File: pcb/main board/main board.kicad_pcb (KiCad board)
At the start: 2 copper layers, 110 x 155 mm, 71 parts, among them J1 Motor 0 Conn, J10 12V Battery, J11 BAU, J12 Servo 4 Conn, J13 Servo 1 Conn, J14 Servo 2 Conn, J15 Servo 3 Conn, J16 Servo 5 Conn, J17 Servo 6 Conn, J18 Servo 7 Conn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

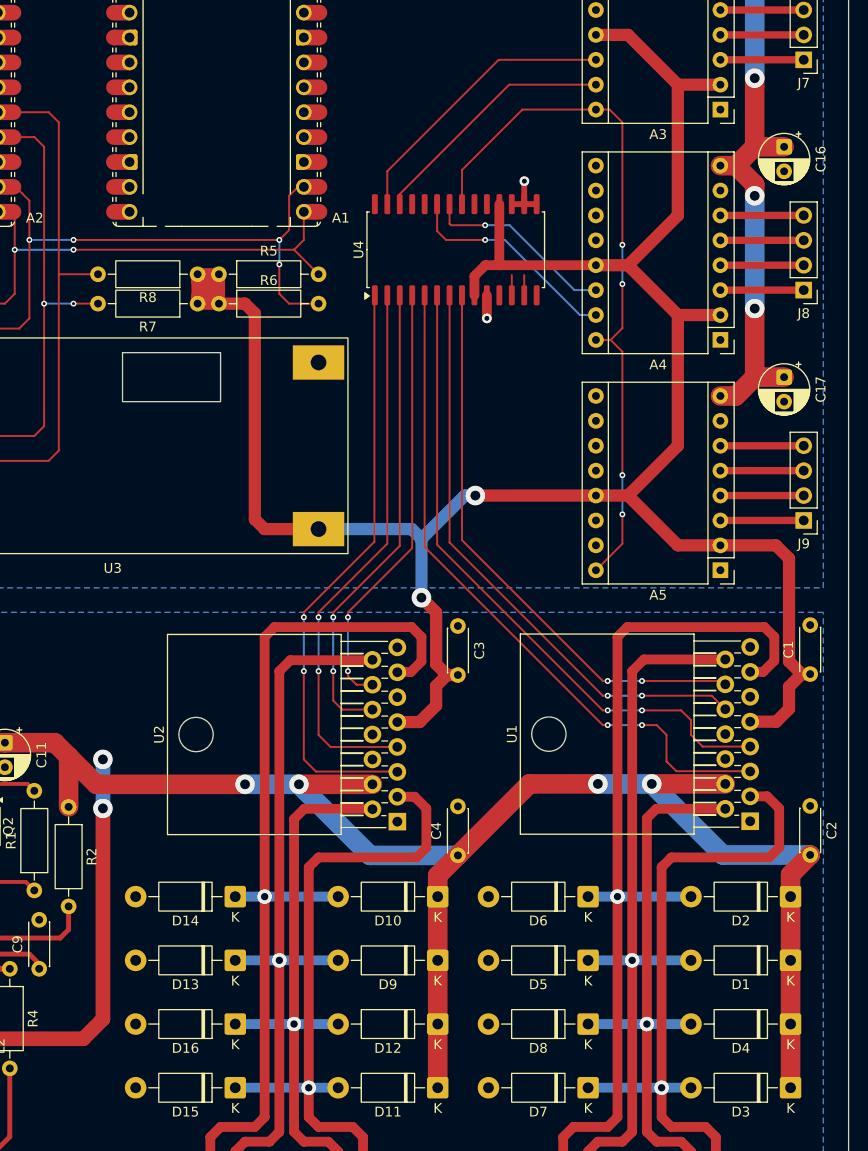
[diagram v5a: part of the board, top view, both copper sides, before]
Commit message: Replaced L298Ns footprints to a vertical version and almost finished rewiring them...
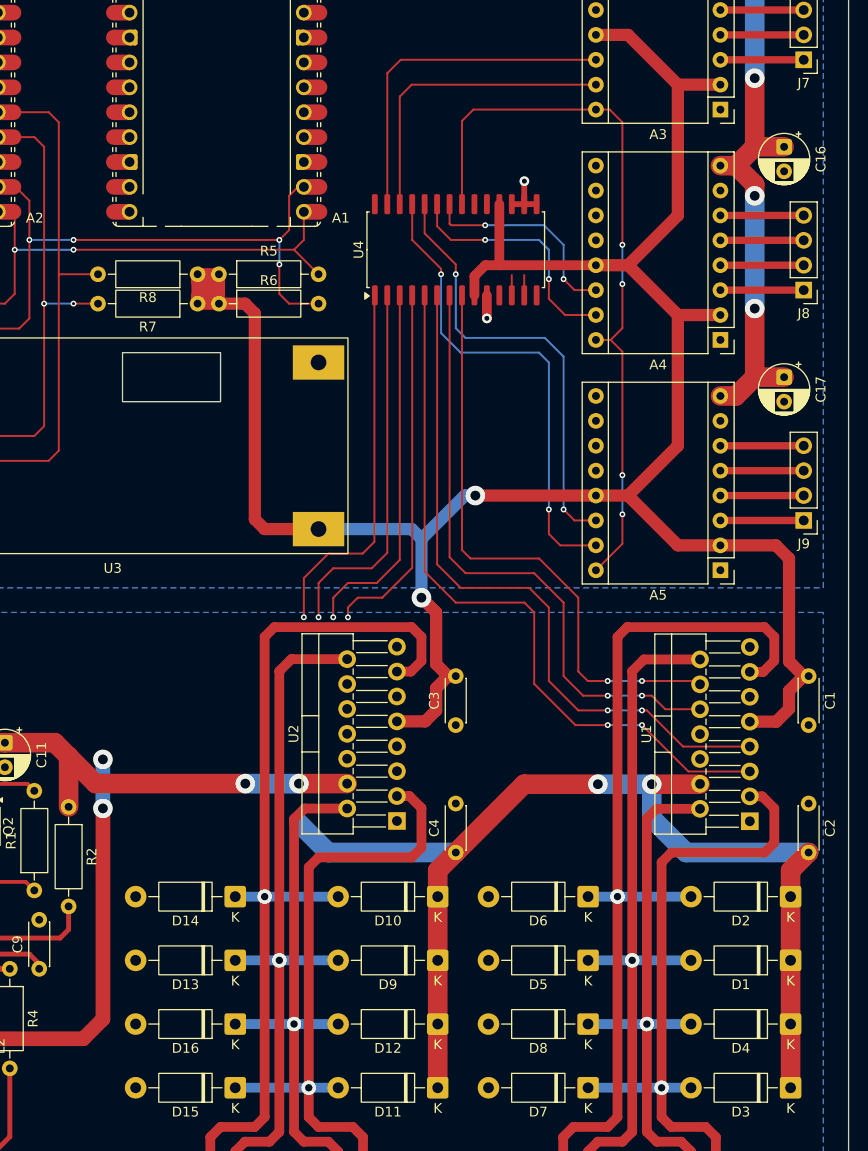
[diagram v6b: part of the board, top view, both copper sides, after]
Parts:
- U1, U2: footprint Package_TO_SOT_THT:TO-220-15_P2.54x2.54mm_StaggerOdd_Lead5.84mm_TabDown -> Package_TO_SOT_THT:TO-220-15_P2.54x5.08mm_StaggerOdd_Lead4.58mm_Vertical
- moved C3 10.1 mm to (247.5, 172.5), turned to 90 degrees
- moved C4 0.37 mm to (247.5, 185.5)
- moved C2 0.30 mm to (283.5, 180.5)
- moved C1 0.26 mm to (283.5, 167.5), turned to -90 degrees
- moved U2 0.08 mm to (241.5, 182.3)
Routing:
- net Stepper 3 Step: track 0.00 -> 49.4 mm, vias 0 -> 2
- net Stepper 3 Sleep: track 0.00 -> 45.5 mm, vias 0 -> 2
- net Motor 3 Direction Pin 1: track 60.4 -> 37.9 mm, vias 2 -> 1
- net Motor 3 Direction Pin 2: track 56.3 -> 38.1 mm, vias 2 -> 1
- net Motor 4 Direction Pin 1: track 48.5 -> 37.4 mm, vias 2 -> 1
- net Motor 4 Direction Pin 2: track 44.4 -> 37.0 mm, vias 2 -> 1
- net Stepper 1 Sleep: track 29.4 -> 35.2 mm
- net Stepper 1 Step: track 25.7 -> 31.5 mm
- net +12V: track 311.4 -> 306.4 mm
- net Motor 1 Direction Pin 2: track 66.8 -> 71.3 mm
- net Motor 1 Direction Pin 1: track 70.0 -> 73.9 mm
- net Steppers Dir: track 72.3 -> 75.2 mm
- net Net-(D1-A): track 74.8 -> 72.1 mm
- net Stepper 2 Step: track 22.5 -> 25.1 mm, vias 1 -> 2
- net Net-(D4-A): track 58.2 -> 55.6 mm
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
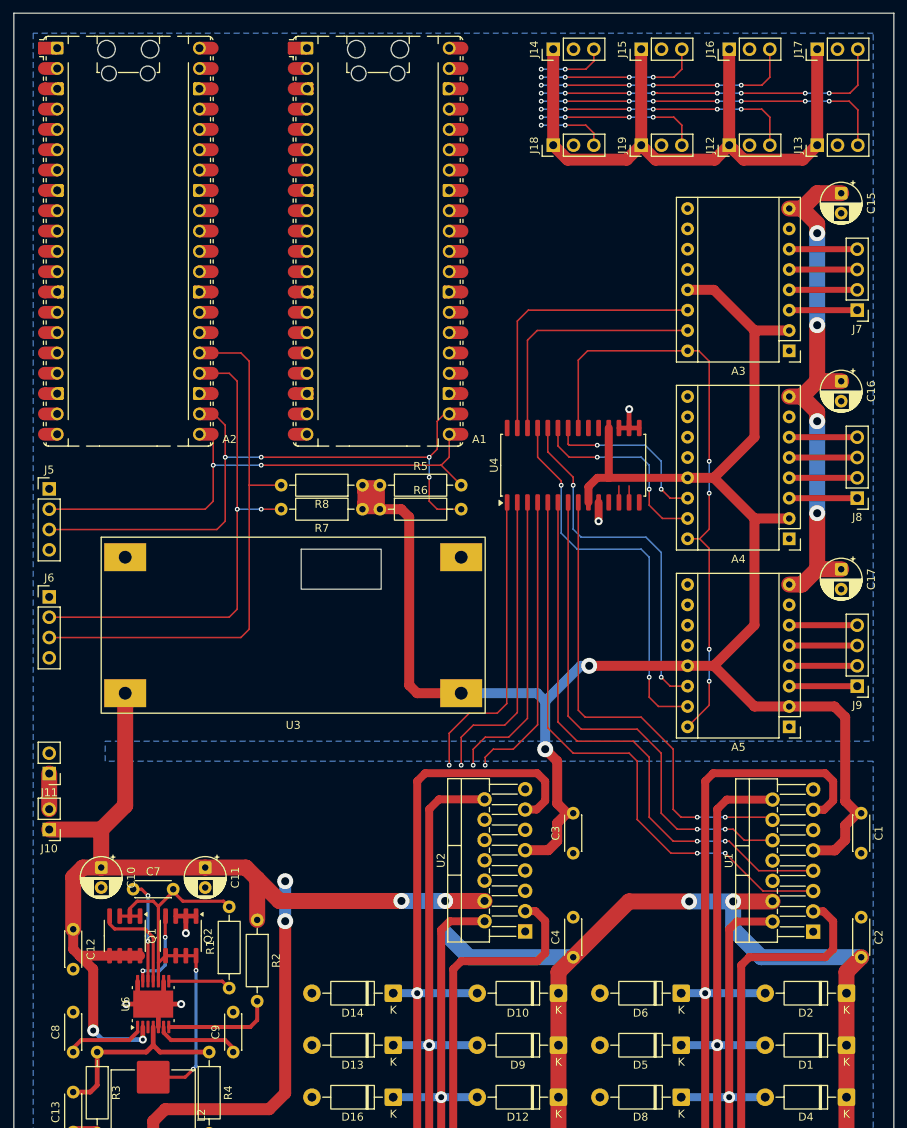
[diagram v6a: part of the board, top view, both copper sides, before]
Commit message: Changed largeur of pistes and finished rewiring DC motors drivers
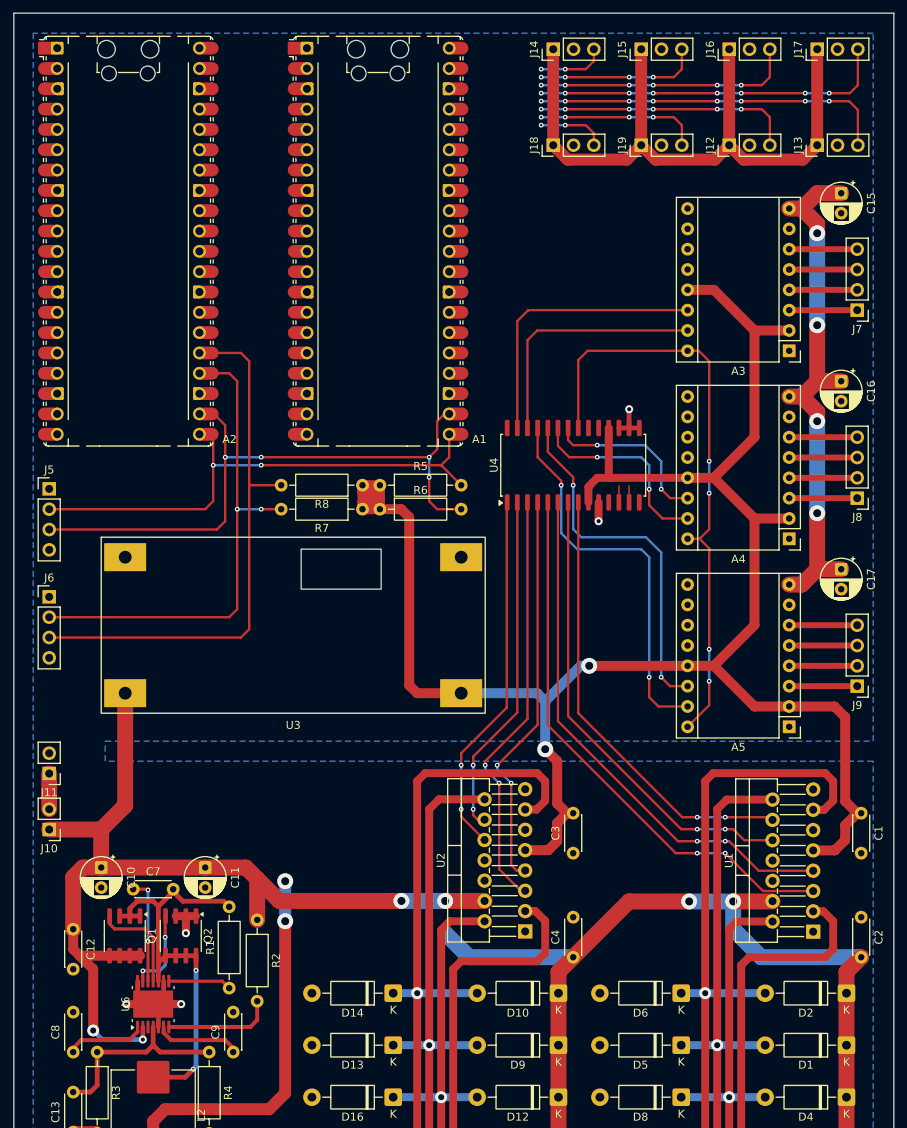
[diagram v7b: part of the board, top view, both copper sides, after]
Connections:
- U4 pad 1: Motor 3 Direction Pin 1 -> Motor 4 Direction Pin 1
- U4 pad 2: Motor 3 Direction Pin 2 -> Motor 4 Direction Pin 2
- U4 pad 3: Motor 4 Direction Pin 1 -> Motor 3 Direction Pin 1
- U4 pad 4: Motor 4 Direction Pin 2 -> Motor 3 Direction Pin 2
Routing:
- net Motor 3 Direction Pin 1: track 37.9 -> 53.1 mm, vias 1 -> 2
- net Motor 3 Direction Pin 2: track 38.1 -> 50.2 mm, vias 1 -> 2
- net Motor 4 Direction Pin 1: track 37.4 -> 45.8 mm, vias 1 -> 2
- net Motor 4 Direction Pin 2: track 37.0 -> 43.0 mm, vias 1 -> 2
- net Motor 1 Direction Pin 1: track 73.9 -> 69.5 mm
- net Motor 1 Direction Pin 2: track 71.3 -> 66.8 mm
- net Motor 2 Direction Pin 1: track 62.9 -> 58.5 mm
- net Motor 2 Direction Pin 2: track 60.2 -> 56.0 mm

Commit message: Almost finished PCB !
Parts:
- A1, A2: footprint Module:RaspberryPi_Pico_Common_Unspecified -> Module:RaspberryPi_Pico_Common_THT
- moved J13 35.2 mm to (245.0, 72.0)
- moved A2 25.8 mm to (182.5, 72.0)
- moved A1 25.5 mm to (214.5, 72.0)
- moved J17 16.3 mm to (267.0, 84.0)
- moved J12 16.3 mm to (278.0, 72.0)
- moved J16 16.3 mm to (278.0, 84.0)
- moved J19 11.0 mm to (245.0, 84.0)
- moved J14 11.0 mm to (256.0, 72.0)
- moved J18 11.0 mm to (256.0, 84.0)
- moved J15 11.0 mm to (267.0, 72.0)
- moved R5 4.70 mm to (222.3, 131.1)
- moved R6 4.70 mm to (222.3, 134.1)
- moved R7 4.70 mm to (220.2, 134.1)
- moved R8 4.70 mm to (220.2, 131.1)
- moved U3 3.91 mm to (209.5, 146.5)
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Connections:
- A1 pad 1: Motor 1 Activation Pin -> Servo 1 PWM
- A1 pad 10: Servo 4 PWM -> Servo 8 PWM
- A1 pad 11: Servo 5 PWM -> Motor 2 Activation Pin
- A1 pad 12: Servo 6 PWM -> Motor 1 Activation Pin
- A1 pad 14: Servo 7 PWM -> Motor 4 Activation Pin
- A1 pad 15: Servo 8 PWM -> Motor 3 Activation Pin
- A1 pad 2: Motor 2 Activation Pin -> Servo 2 PWM
- A1 pad 4: Motor 3 Activation Pin -> Servo 3 PWM
- A1 pad 5: Motor 4 Activation Pin -> Servo 4 PWM
- A1 pad 6: Servo 1 PWM -> Servo 5 PWM
- A1 pad 7: Servo 2 PWM -> Servo 6 PWM
- A1 pad 9: Servo 3 PWM -> Servo 7 PWM
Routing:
- net Motor 1 Activation Pin: track 0.00 -> 131.4 mm, vias 0 -> 9
- net Motor 2 Activation Pin: track 0.00 -> 127.8 mm, vias 0 -> 8
- net Motor 4 Activation Pin: track 0.00 -> 90.2 mm, vias 0 -> 7
- net Motor 3 Activation Pin: track 0.00 -> 88.1 mm, vias 0 -> 6
- net +5VL: track 240.9 -> 325.6 mm, vias 2 -> 3
- net Servo 7 PWM: track 8.49 -> 54.3 mm, vias 2 -> 4
- net Servo 5 PWM: track 32.5 -> 76.0 mm, vias 6 -> 8
- net Servo 4 PWM: track 32.5 -> 75.9 mm, vias 6 -> 8
- net Servo 3 PWM: track 20.5 -> 62.7 mm, vias 4 -> 6
- net Servo 2 PWM: track 8.49 -> 50.2 mm, vias 2 -> 4
- net Servo 8 PWM: track 20.5 -> 43.0 mm, vias 4 -> 2
- net Servo 6 PWM: track 45.0 -> 64.6 mm, vias 8 -> 6
- net Servo 1 PWM: track 44.4 -> 38.5 mm, vias 8 -> 2
- net I2C 0 SDA: track 69.0 -> 74.0 mm
- net +12V: track 306.4 -> 302.5 mm
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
